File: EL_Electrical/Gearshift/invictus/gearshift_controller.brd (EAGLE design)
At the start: 160 x 100 mm, 55 parts, among them IC1 MCP2562-E_SN, IC2 MCP2515-I_SO, J1 22-05-7028-02, Q1 BSS123, Q2 BSS123, Q3 BSS123, Q4 BSS123, Q5 BSS123, Q6 BSS123, Q7 BSS123

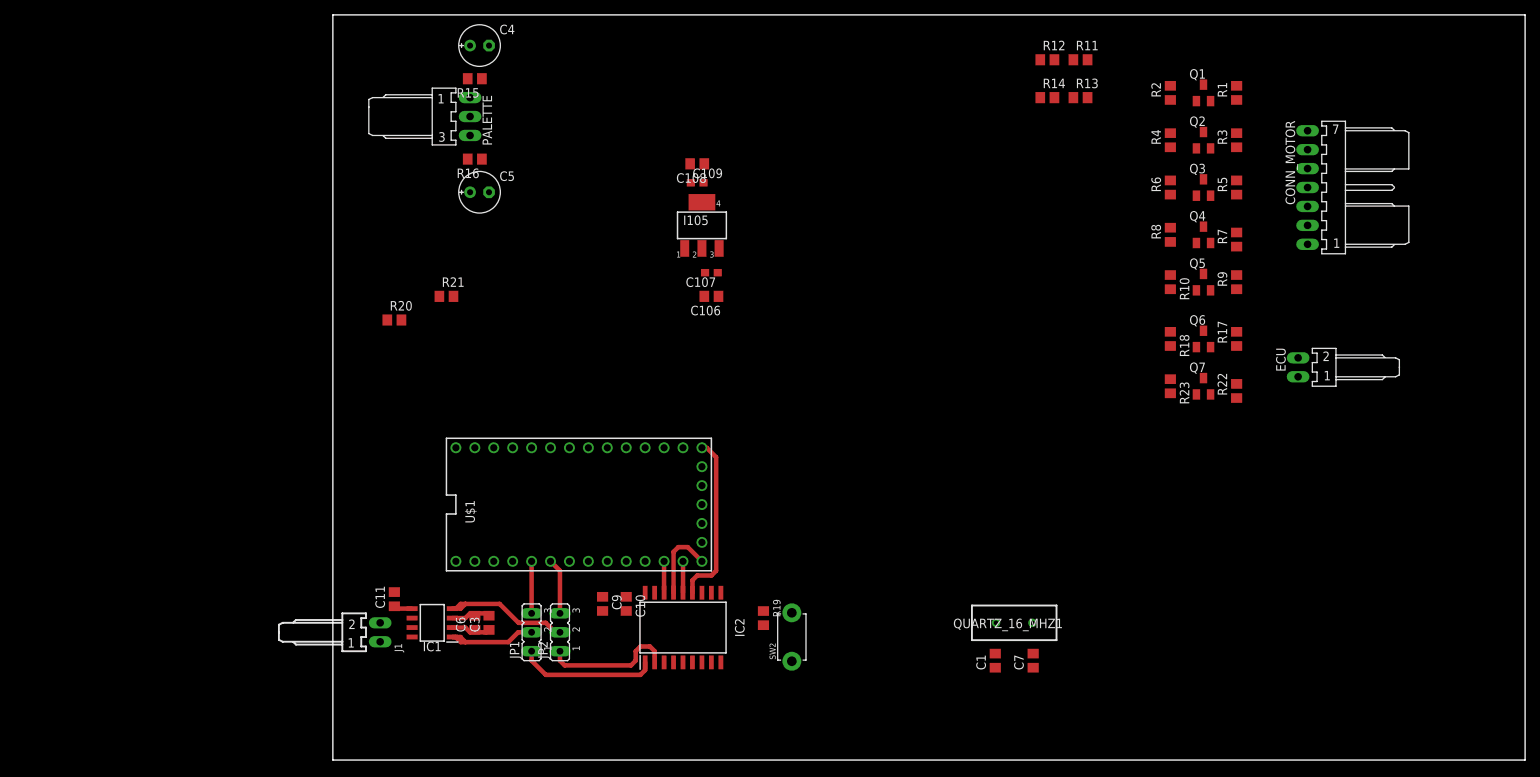
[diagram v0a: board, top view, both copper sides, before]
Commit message: Update of electrical schematic (4 pins from DTA extras)
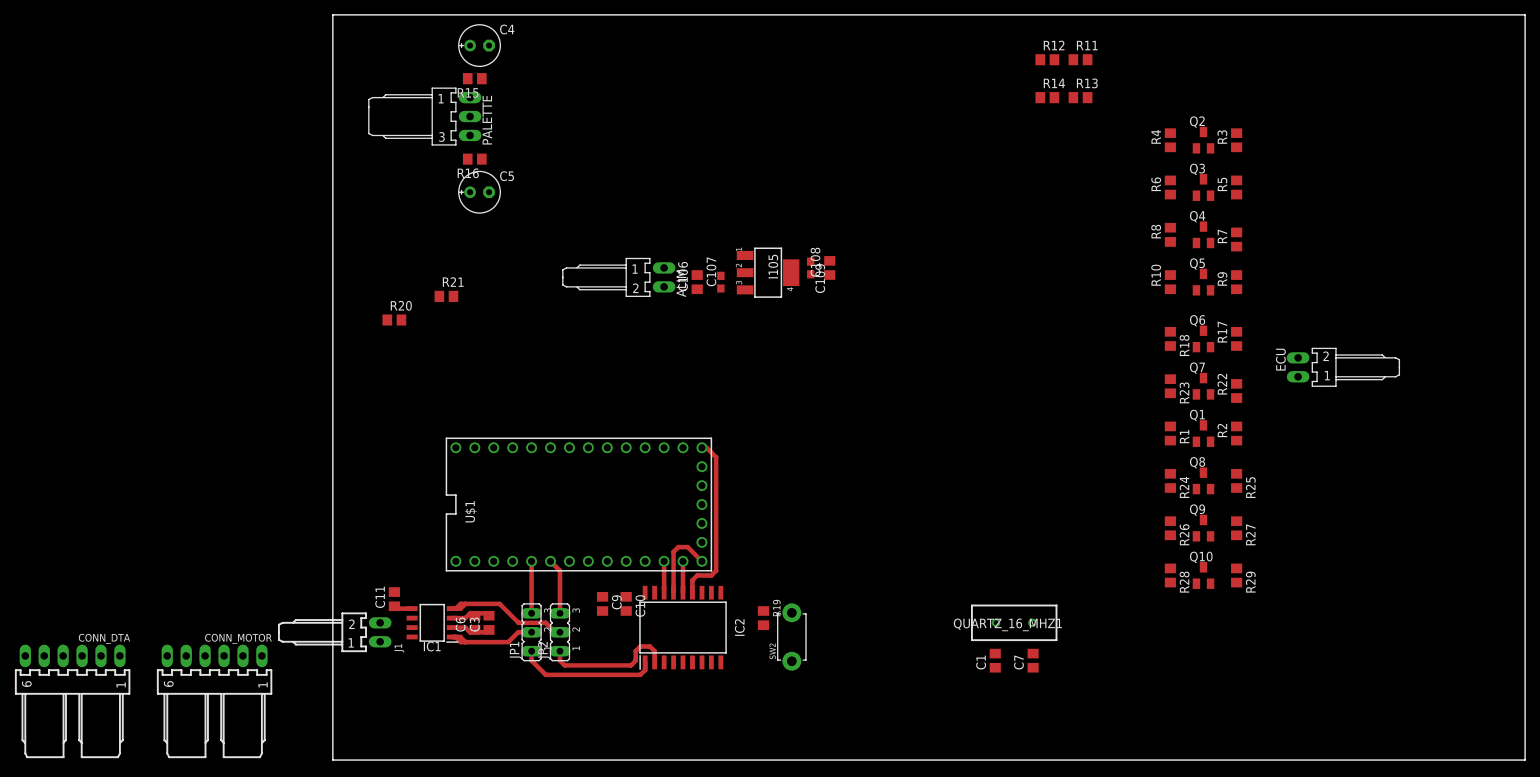
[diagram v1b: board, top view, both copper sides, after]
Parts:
- added ALIM: 22-05-7028-02, EP_molex_6410_7395:7395-02
- added CONN_DTA: 22-05-7068-06, con-molex:7395-06
- added Q10, Q8, Q9: BSS123, transistor-small-signal:SOT23
- added R24, R25, R26, R27, R28, R29: 10k, rcl:R0805
- CONN_MOTOR: value 22-05-7078-07 -> 22-05-7068-06; device EP_molex_6410_7395:7395-07 -> con-molex:7395-06
- moved CONN_MOTOR 159.6 mm to (-15.9, 14.0), turned to 0 degrees
- moved R1 46.6 mm to (112.4, 43.8), turned to 270 degrees
- moved R2 46.6 mm to (121.3, 43.8)
- moved Q1 45.7 mm to (116.8, 43.8)
- moved C108 22.6 mm to (66.7, 66.0), turned to 90 degrees
- moved C109 19.0 mm to (64.1, 66.0), turned to 270 degrees
- moved I105 10.9 mm to (58.4, 65.4), turned to 270 degrees
- moved C106 2.69 mm to (48.9, 64.1), turned to 90 degrees
- moved C107 1.80 mm to (52.1, 64.1), turned to 90 degrees
- turned R10 to 90 degrees
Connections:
- net OUT0_3.3V renamed LOG_3.3V
- net SHIFT_POT_5V renamed GEAR_POT_5V
- removed net OUT0_12V: CONN_MOTOR.5, Q1.3, R2.1
- removed net SHIFT_POT_3.3V: Q5.2, Q7.2, R22.1, R9.1
- new net GEAR_POT_3.3V: Q7.2, R22.1
- new net LAUNCH_CONTROL_3.3V: Q9.2, R26.1
- new net LAUNCH_CONTROL_5V: Q9.3, R27.1
- new net LOG_5V: Q1.3, R2.1
- new net N$1: CONN_DTA.1
- new net N$10: CONN_DTA.5
- new net N$12: CONN_DTA.6
- new net N$5: CONN_DTA.2
- new net N$8: CONN_DTA.3
- new net N$9: CONN_DTA.4
- new net OUT3_3.3V: Q4.2, R7.1
- new net OUT4_3.3V: Q5.2, R9.1
- new net TRACTION_CONTROL_3.3V: Q8.2, R24.1
- new net TRACTION_CONTROL_5V: Q8.3, R25.1
- new net WET/DRY_3.3V: Q10.2, R28.1
- new net WET/DRY_5V: Q10.3, R29.1
- net +12V: now also ALIM.2; no longer R2.2
- net +3V3: now also Q10.1, Q8.1, Q9.1, R24.2, R26.2, R28.2
- net +5V: now also R2.2, R25.2, R27.2, R29.2
- net GND: now also ALIM.1
- net IN0_12V: now also CONN_MOTOR.6; no longer CONN_MOTOR.7
- net IN1_12V: now also CONN_MOTOR.5; no longer CONN_MOTOR.6
- net SHIFT_CUT_3.3V: no longer Q4.2, R7.1

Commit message: Definition of inputs/outputs in Teensy 3.2. PCB Layout Design (ground plane missing)
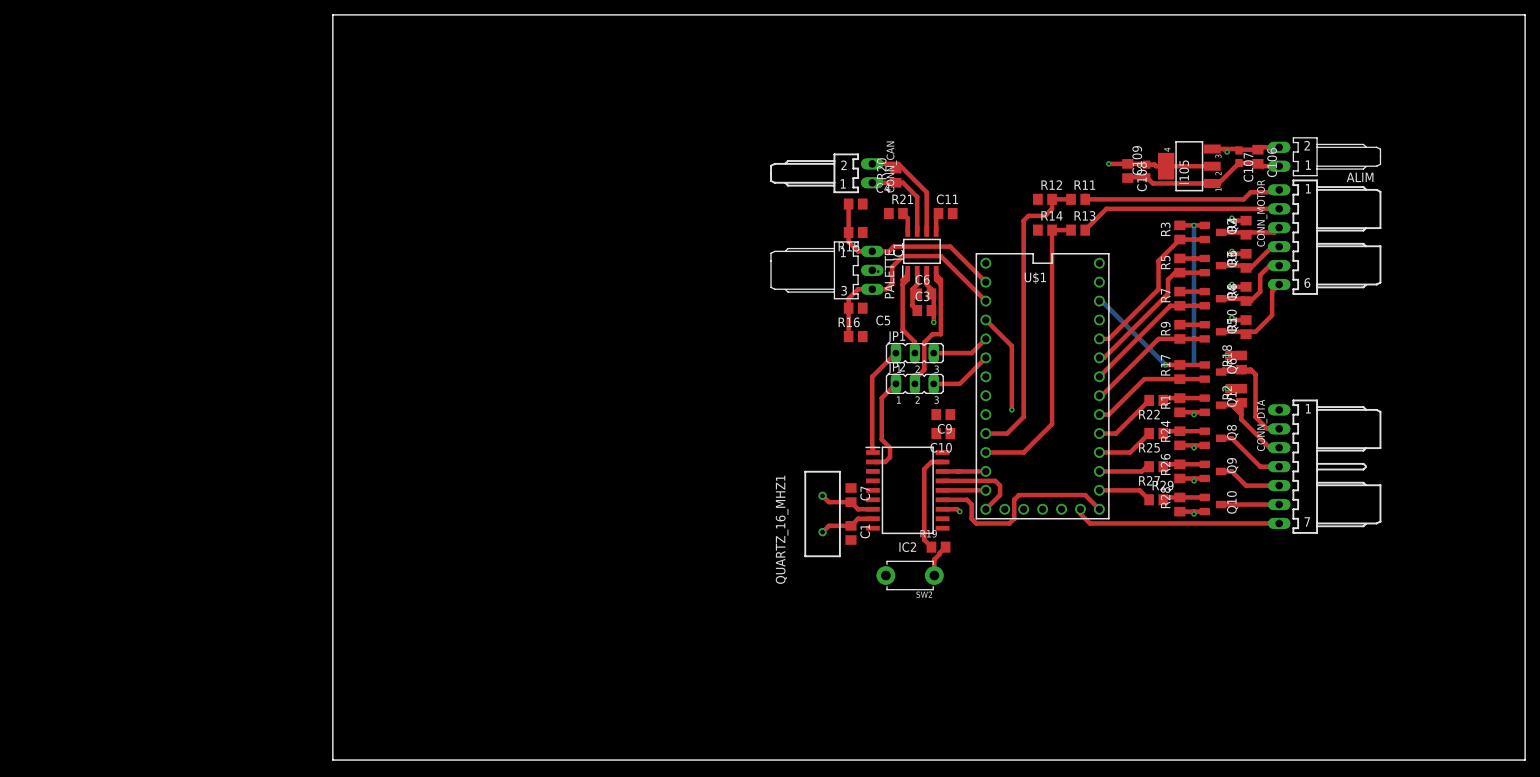
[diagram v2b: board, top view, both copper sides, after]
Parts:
- removed ECU: 22-05-7028-02, EP_molex_6410_7395:7395-02
- removed J1: 22-05-7028-02, con-molex:7395-02
- removed Q7: BSS123, transistor-small-signal:SOT23
- removed R23: 10k, rcl:R0805
- added CONN_CAN: 22-05-7028-02, con-molex:7395-02
- C4, C5: device rcl:E2,5-6E -> rcl:C0805
- CONN_DTA: value 22-05-7068-06 -> 22-05-7078-07; device con-molex:7395-06 -> con-molex:7395-07
- Q1, Q10, Q2, Q3, Q4, Q5, Q6, Q9: value BSS123 -> BSS138
- R2: value 10k -> 4k7
- R22, R25, R27, R29: value 10k -> 330
- moved CONN_DTA 163.9 mm to (127.0, 39.4), turned to 90 degrees
- moved CONN_MOTOR 153.5 mm to (127.0, 70.2), turned to 90 degrees
- moved C11 90.3 mm to (82.2, 73.3), turned to 0 degrees
- moved ALIM 84.1 mm to (127.0, 81.0), turned to 270 degrees
- moved IC1 82.5 mm to (79.1, 68.3), turned to 90 degrees
- moved C106 77.1 mm to (124.1, 81.0), turned to 270 degrees
- moved C6 74.7 mm to (79.4, 62.5), turned to 0 degrees
- moved C3 71.9 mm to (79.4, 60.3), turned to 0 degrees
- moved C107 71.5 mm to (121.6, 81.0), turned to 270 degrees
- moved R20 70.0 mm to (75.6, 78.4), turned to 90 degrees
- moved U$1 64.2 mm to (95.2, 50.2), turned to 0 degrees
- moved JP1 63.6 mm to (78.1, 54.6), turned to 0 degrees
- moved R21 61.3 mm to (75.6, 73.3)
- moved I105 58.3 mm to (114.9, 79.7), turned to 90 degrees
- moved JP2 58.1 mm to (78.1, 50.5), turned to 0 degrees
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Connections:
- removed net GEAR_POT_3.3V: Q7.2, R22.1
- removed net GEAR_POT_5V: ECU.1, Q7.3, R23.1
- removed net N$12: CONN_DTA.6
- removed net N$5: CONN_DTA.2
- new net GEAR_POT: CONN_DTA.7, U$1.RESET/DAC
- new net GND1: CONN_DTA.1, Q1.2, Q10.2, Q8.2, Q9.2, R1.1, R24.1, R26.1, R28.1
- net +3V3: no longer Q1.1, Q10.1, Q7.1, Q8.1, Q9.1, R1.2, R22.2, R24.2, R26.2, R28.2
- net +5V: no longer R23.2, R25.2, R27.2, R29.2
- net GND: now also C4.2, C5.2; no longer C4.-, C5.-
- net IN0_12V: now also CONN_MOTOR.1; no longer CONN_MOTOR.6
- net IN0_3.3V: now also U$1.8
- net IN1_12V: now also CONN_MOTOR.2; no longer CONN_MOTOR.5
- net IN1_3.3V: now also U$1.9
- net LAUNCH_CONTROL_3.3V: now also R27.2, U$1.15/A1; no longer Q9.2, R26.1
- net LAUNCH_CONTROL_5V: now also CONN_DTA.5; no longer R27.1
- net LOG_3.3V: now also R22.2, U$1.17/A3; no longer Q1.2, R1.1
- net LOG_5V: now also CONN_DTA.3
- net N$1: now also Q1.1, R1.2, R22.1; no longer CONN_DTA.1
- net N$10: now also Q10.1, R28.2, R29.2; no longer CONN_DTA.5
- net N$4: now also CONN_CAN.1; no longer J1.2
- net N$6: now also CONN_CAN.2; no longer J1.1
- net N$8: now also Q8.1, R24.2, R25.1; no longer CONN_DTA.3
- net N$9: now also Q9.1, R26.2, R27.1; no longer CONN_DTA.4
- net OUT1_12V: now also CONN_MOTOR.3; no longer CONN_MOTOR.4
- net OUT1_3.3V: now also U$1.22/A8
- net OUT2_12V: now also CONN_MOTOR.4; no longer CONN_MOTOR.3
- net OUT2_3.3V: now also U$1.21/A7
- net OUT3_12V: now also CONN_MOTOR.5; no longer CONN_MOTOR.2
- net OUT3_3.3V: now also U$1.20/A6
- net OUT4_12V: now also CONN_MOTOR.6; no longer CONN_MOTOR.1
- net OUT4_3.3V: now also U$1.19/A5
- net PALETTE_DROITE: now also C5.1, U$1.1; no longer C5.+
- net PALETTE_GAUCHE: now also C4.1, U$1.0; no longer C4.+
- net SHIFT_CUT_3.3V: now also U$1.18/A4
- net SHIFT_CUT_5V: now also CONN_DTA.2; no longer ECU.2
- net TRACTION_CONTROL_3.3V: now also R25.2, U$1.16/A2; no longer Q8.2, R24.1
- net TRACTION_CONTROL_5V: now also CONN_DTA.4; no longer R25.1
- net WET/DRY_3.3V: now also R29.1, U$1.14/A0; no longer Q10.2, R28.1
- net WET/DRY_5V: now also CONN_DTA.6; no longer R29.1
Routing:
- net +5V: track 4.81 -> 122.3 mm, vias 0 -> 5
- net +3V3: track 2.51 -> 52.3 mm, vias 0 -> 2
- net +12V: track 0.00 -> 41.1 mm, vias 0 -> 5
- net IN0_3.3V: track 0.00 -> 40.6 mm
- net GND1: track 0.00 -> 39.7 mm, vias 0 -> 4
- net IN1_3.3V: track 0.00 -> 39.0 mm
- net INT: track 0.00 -> 38.9 mm, vias 0 -> 2
- net PALETTE_DROITE: track 0.00 -> 29.7 mm
- net GEAR_POT: track 0.00 -> 27.8 mm
- net IN1_12V: track 0.00 -> 27.5 mm
- net IN0_12V: track 0.00 -> 27.1 mm
- net PALETTE_GAUCHE: track 0.00 -> 26.3 mm
- net GND: track 5.32 -> 27.8 mm
- net OUT1_3.3V: track 0.00 -> 21.9 mm
- net OUT2_3.3V: track 0.00 -> 20.0 mm
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
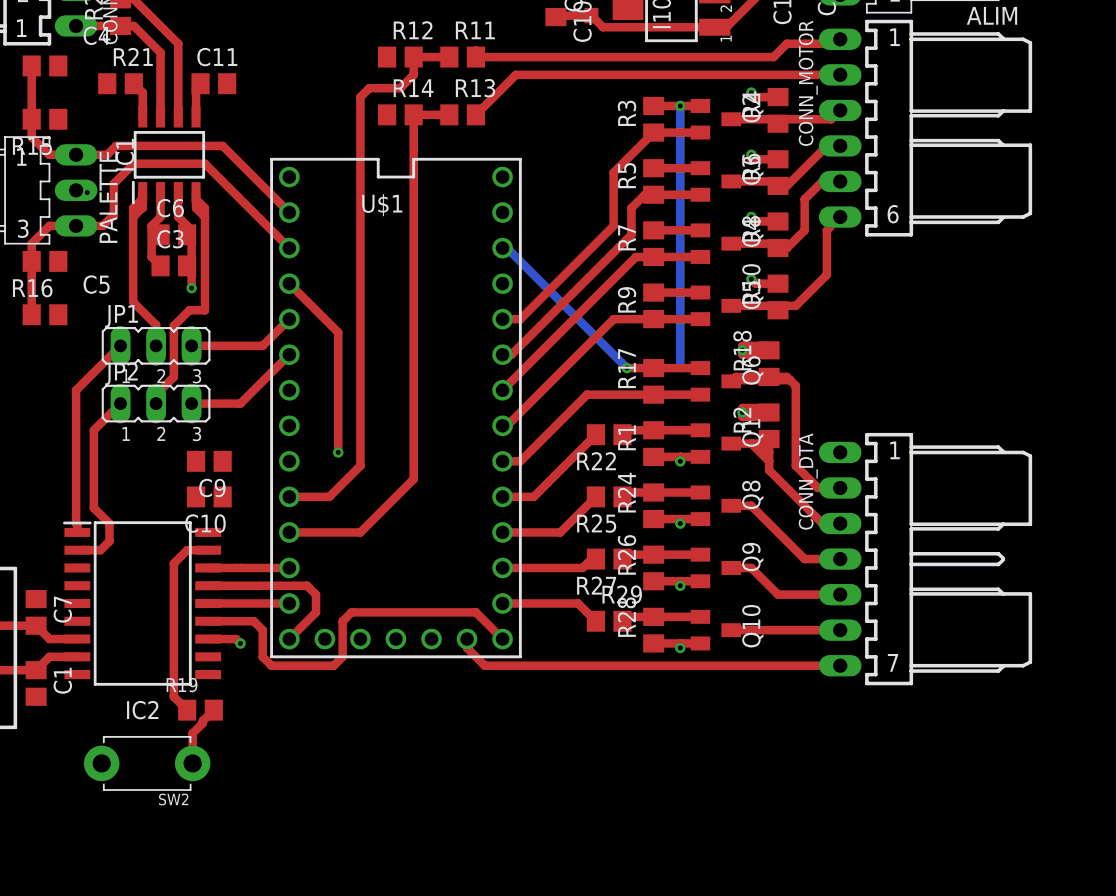
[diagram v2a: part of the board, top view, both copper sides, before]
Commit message: Update de sch et brd files (Position of connectors, minor changes)
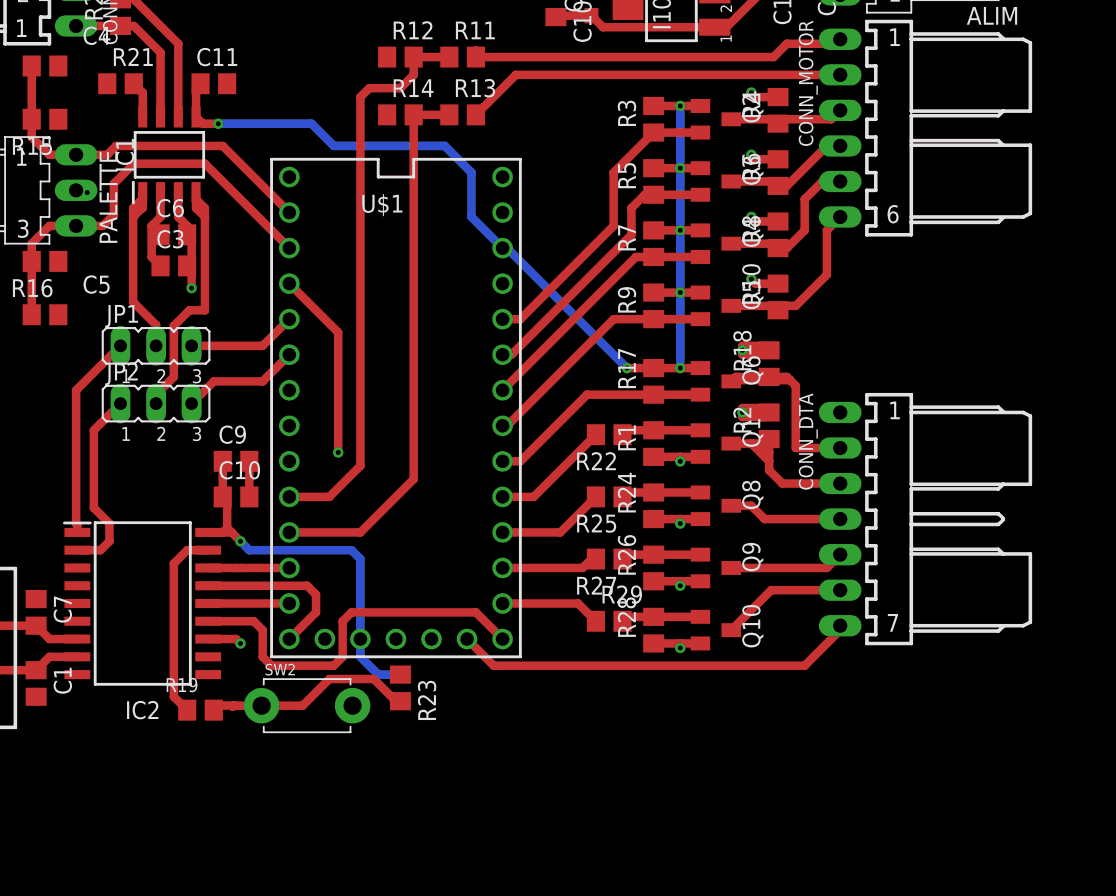
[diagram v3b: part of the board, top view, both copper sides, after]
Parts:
- added R23: 1k, rcl:R0805
- moved SW2 12.2 mm to (88.9, 28.9), turned to 0 degrees
- moved CONN_DTA 2.86 mm to (127.0, 42.2)
- moved C10 1.90 mm to (83.8, 43.8), turned to 0 degrees
- moved C9 1.90 mm to (83.8, 46.4), turned to 0 degrees
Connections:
- net +3V3: now also R23.1
- net RESET: now also R23.2
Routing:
- net +3V3: track 52.3 -> 107.0 mm, vias 2 -> 8
- net RESET: track 4.44 -> 15.1 mm
- net GND1: track 39.7 -> 31.5 mm
- net GND: track 27.8 -> 30.8 mm
- net SHIFT_CUT_5V: track 18.7 -> 16.8 mm
- net TRACTION_CONTROL_5V: track 9.37 -> 8.18 mm
- net WET/DRY_5V: track 7.79 -> 8.97 mm
- net LOG_5V: track 13.7 -> 12.5 mm
- net GEAR_POT: track 27.8 -> 28.8 mm
- added copper zone on layer 2, net GND1
